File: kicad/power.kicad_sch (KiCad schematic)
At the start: 44 parts, among them Q1 BC857, Q2 BC847, Q3 BC857, U4 AP62201-SOT563, U5 AP62201-SOT563, U6 TLV71x, U7 TLV71x

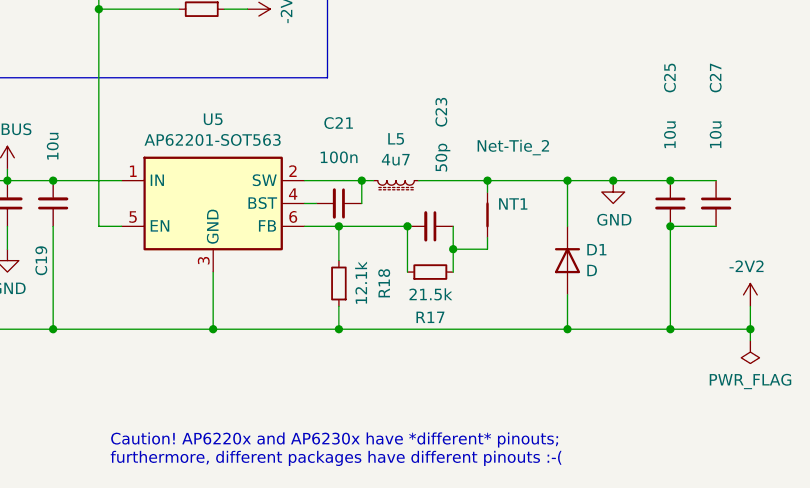
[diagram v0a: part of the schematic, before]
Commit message: modified a few values (as loaded on v2 prototype board)
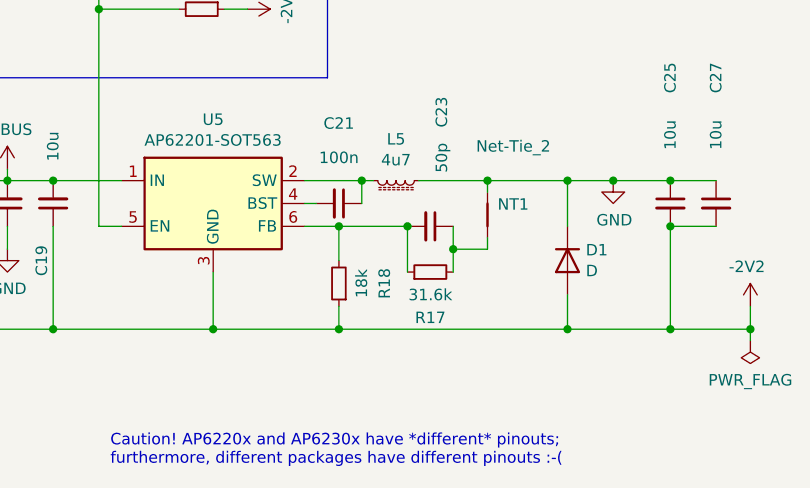
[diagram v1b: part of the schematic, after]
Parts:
- R17: value 21.5k -> 31.6k
- R18: value 12.1k -> 18k
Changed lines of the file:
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@@
       (effects (font (size 1.27 1.27)))
     )
-    (property "Value" "21.5k" (at 99.06 153.67 90)
+    (property "Value" "31.6k" (at 99.06 153.67 90)
       (effects (font (size 1.27 1.27)))
     )
@@
       (effects (font (size 1.27 1.27)))
     )
-    (property "Value" "12.1k" (at 91.44 152.4 90)
+    (property "Value" "18k" (at 91.44 152.4 90)
       (effects (font (size 1.27 1.27)))
     )

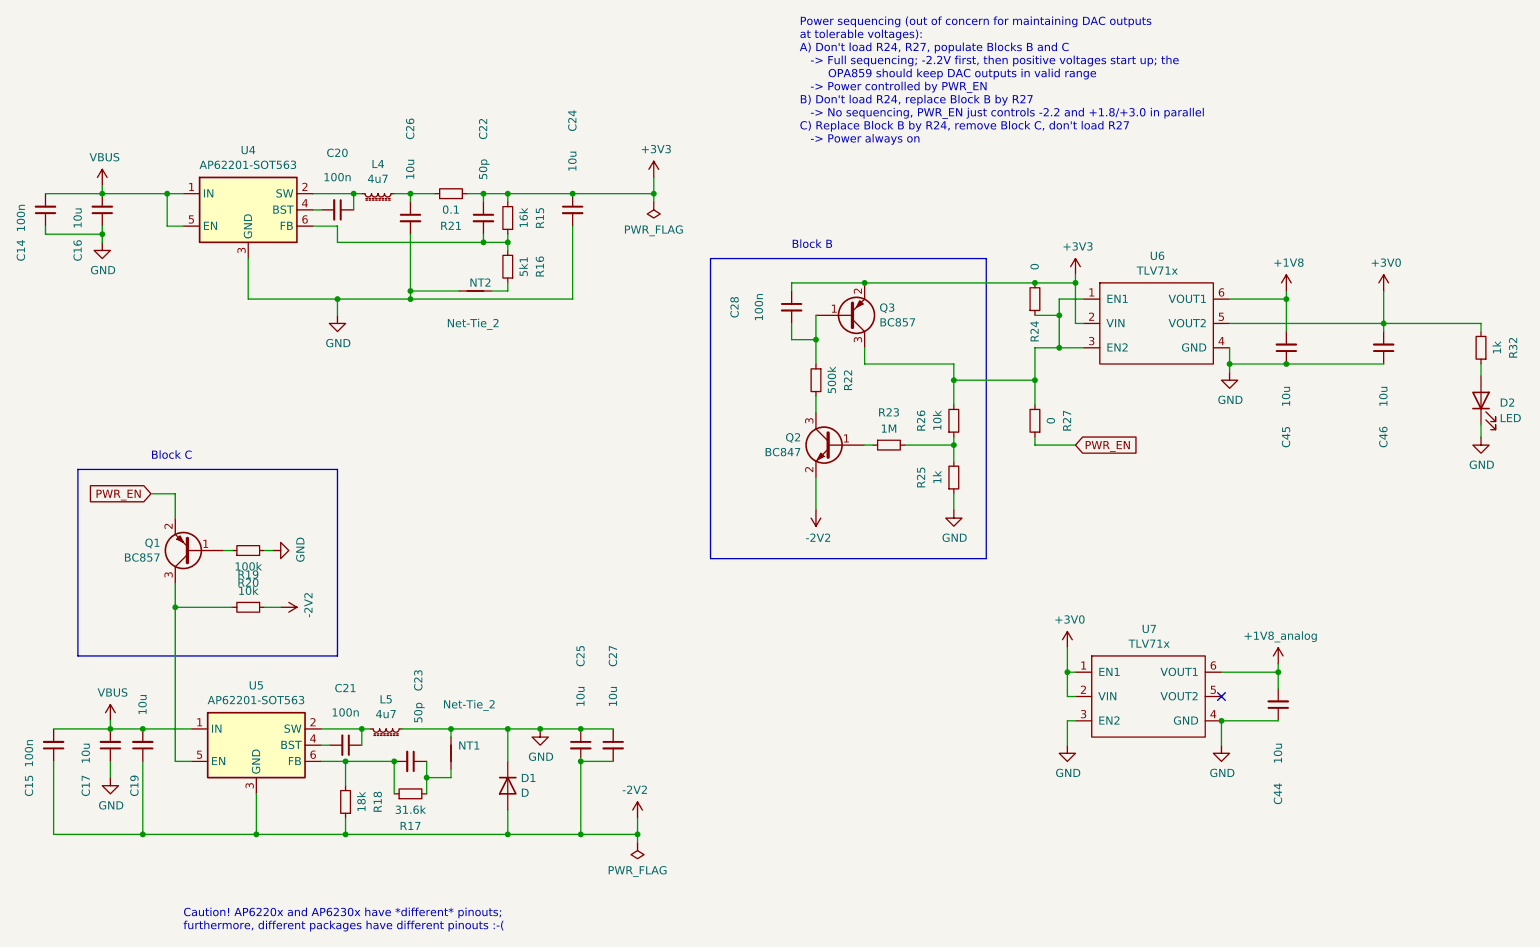
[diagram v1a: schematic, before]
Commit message: changed values in schematic for v2 board
Most notably: moved from +3.0/-2.2V to +2.8/-2.4V analog supply.
This required changing the diff-amp resistors to stay within
the common-mode range of the AD9954 and the OPA859.
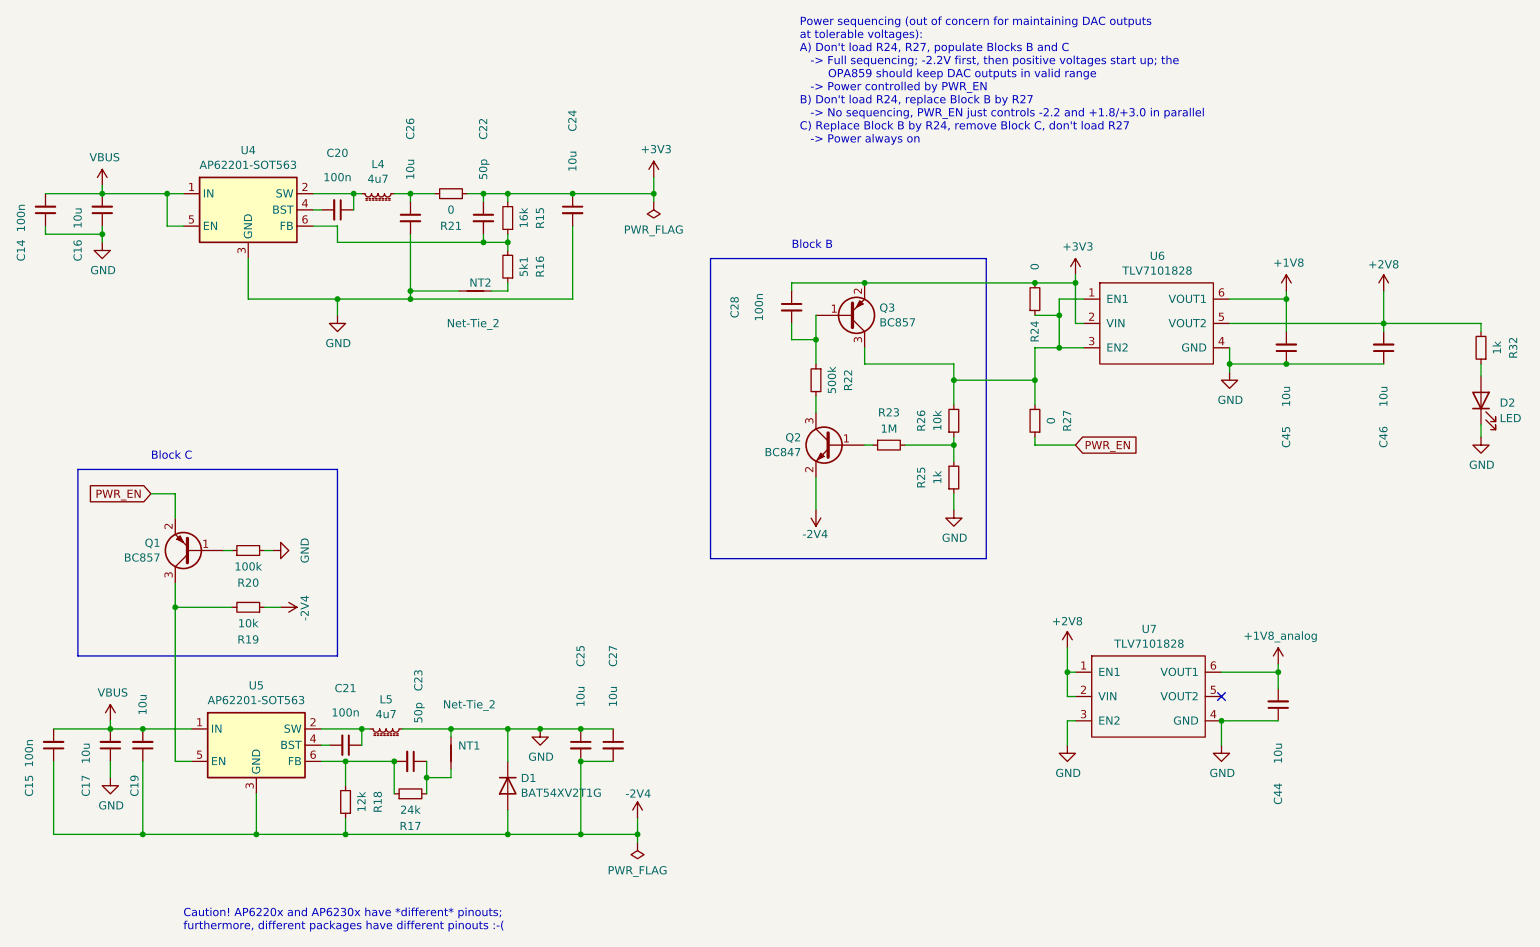
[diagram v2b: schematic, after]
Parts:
- D1: value D -> BAT54XV2T1G
- R17: value 31.6k -> 24k
- R18: value 18k -> 12k
- R21: value 0.1 -> 0
- U6, U7: value TLV71x -> TLV7101828
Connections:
- net +3V0 renamed +2V8
- net -2V2 renamed -2V4
